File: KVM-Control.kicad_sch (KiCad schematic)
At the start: 0 parts

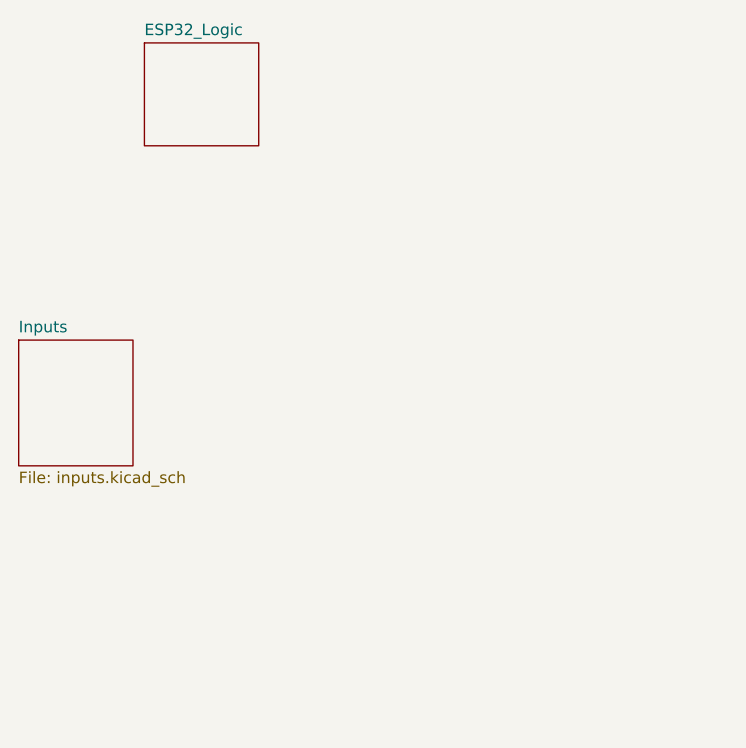
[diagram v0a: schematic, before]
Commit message: Added status LEDs.
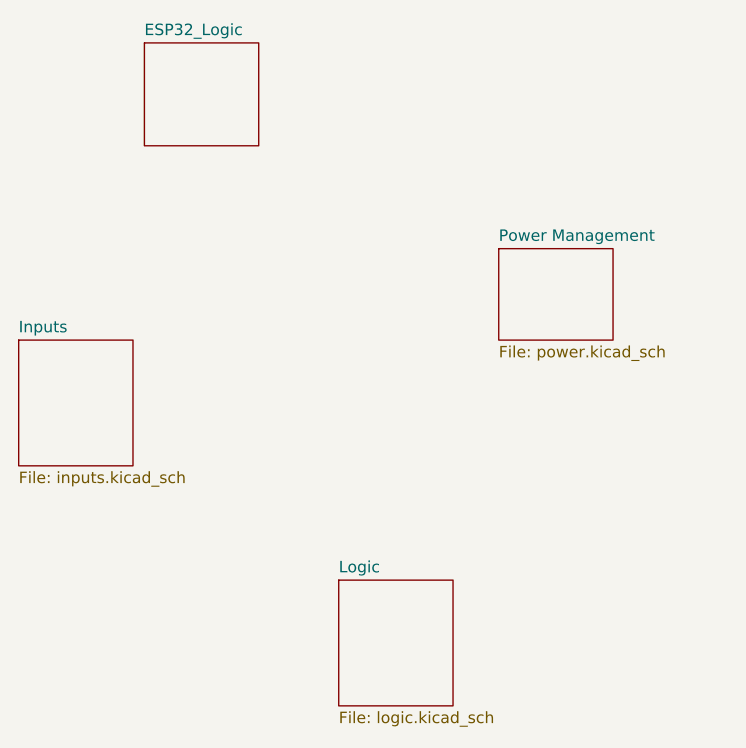
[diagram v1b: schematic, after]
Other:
- added sheet Logic (logic.kicad_sch)
- added sheet Power Management (power.kicad_sch)
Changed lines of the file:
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@@
 	(paper "A4")
+	(sheet
+		(at 73.66 97.79)
+		(size 12.7 13.97)
+		(exclude_from_sim no)
+		(in_bom yes)
+		(on_board yes)
+		(dnp no)
+		(fields_autoplaced yes)
+		(stroke
+			(width 0.1524)
+			(type solid)
+		)
+		(fill
+			(color 0 0 0 0.0000)
+		)
+		(property "Sheetname" "Logic"
+			(at 73.66 97.0784 0)
+			(effects
+				(font
+					(size 1.27 1.27)
+				)
+				(justify left bottom)
+			)
+		)
+		(property "Sheetfile" "logic.kicad_sch"
+			(at 73.66 112.3446 0)
+			(effects
+				(font
+					(size 1.27 1.27)
+				)
+				(justify left top)
+			)
+		)
+		(instances
+			(project "KVM-Control"
+				(path "/ffa57959-0cb1-434b-ad03-c55af2413b19"
+					(page "5")
+				)
+			)
+		)
+	)
 	(sheet
 		(at 52.07 38.1)
@@
 				)
 			)
+		)
+	)
+	(sheet
+		(at 91.44 60.96)
+		(size 12.7 10.16)
+		(exclude_from_sim no)
+		(in_bom yes)
+		(on_board yes)
+		(dnp no)
+		(fields_autoplaced yes)
+		(stroke
+			(width 0.1524)
+			(type solid)
+		)
+		(fill
+			(color 0 0 0 0.0000)
+		)
+		(property "Sheetname" "Power Management"
+			(at 91.44 60.2484 0)
+			(effects
+				(font
+					(size 1.27 1.27)
+				)
+				(justify left bottom)
+			)
+		)
+		(property "Sheetfile" "power.kicad_sch"
+			(at 91.44 71.7046 0)
+			(effects
+				(font
+					(size 1.27 1.27)
+				)
+				(justify left top)
+			)
+		)
+		(instances
+			(project "KVM-Control"
+				(path "/ffa57959-0cb1-434b-ad03-c55af2413b19"
+					(page "4")
+				)
+			)
